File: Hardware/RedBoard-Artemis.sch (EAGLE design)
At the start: 84 parts, among them IC3 LM1117, J2 CORTEX_DEBUG, J3 POWER_JACKTOE, J5 USB-C, Q1 1.1A/60V/600mΩ, U1 ARTEMIS_MODULESMD, U3 AP2112-3.3V, U5 CH340C, Y1 32.768kHz

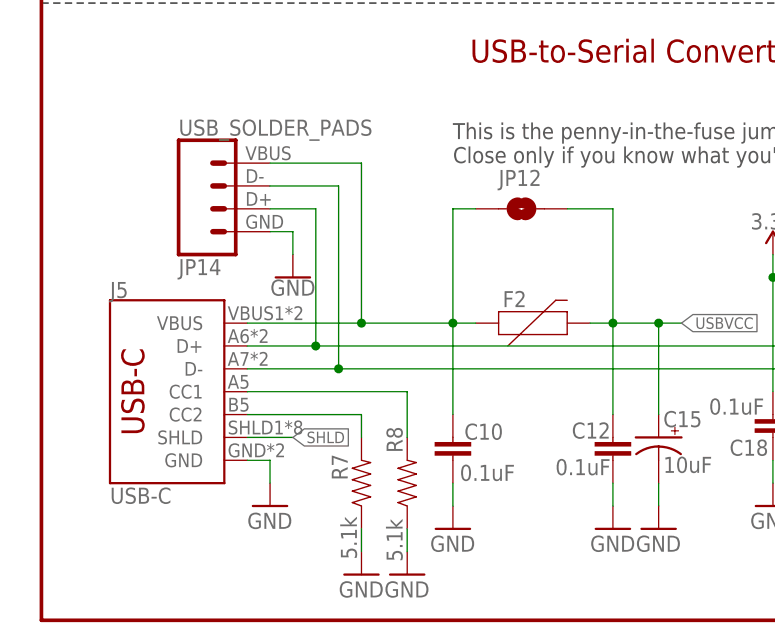
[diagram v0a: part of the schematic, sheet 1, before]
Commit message: Move measurement PTH from under CR2032.
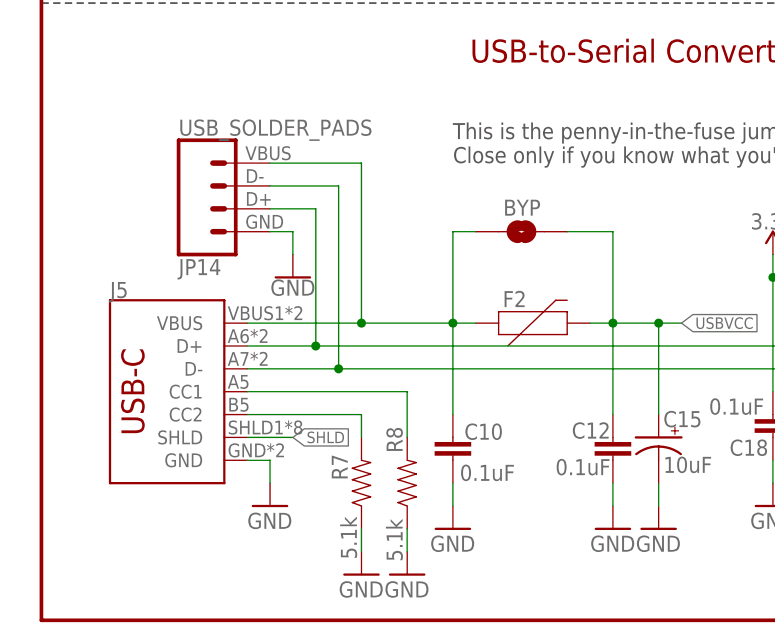
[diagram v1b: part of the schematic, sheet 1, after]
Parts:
- removed JP12: JUMPER-SMT_2_NO_SILK, SparkFun-Jumpers:JUMPER-SMT_2_NO_SILK
- added BYP: JUMPER-SMT_2_NO_SILK, SparkFun-Jumpers:JUMPER-SMT_2_NO_SILK
- J5: device SparkFun-Connectors:USB_C -> SparkFun-Connectors:USB_C2-LAYER
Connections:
- net USBVCC: now also BYP.2; no longer JP12.2
- net VUSB: now also BYP.1; no longer JP12.1
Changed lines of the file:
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@@
 <part name="R16" library="SparkFun-Resistors" deviceset="4.7KOHM" device="-0603-1/10W-1%" value="4.7k"/>
 <part name="D2" library="SparkFun-LED" deviceset="LED-GREEN" device="LILYPAD" value="GREEN"/>
-<part name="J5" library="SparkFun-Connectors" deviceset="USB_C" device="" value="USB-C"/>
+<part name="J5" library="SparkFun-Connectors" deviceset="USB_C" device="2-LAYER" value="USB-C"/>
 <part name="GND38" library="SparkFun-PowerSymbols" deviceset="GND" device=""/>
 <part name="U5" library="SparkFun-IC-Comms" deviceset="CH340C" device=""/>
@@
 <part name="JP14" library="SparkFun-Connectors" deviceset="USB_SOLDER_PADS" device=""/>
 <part name="GND17" library="SparkFun-PowerSymbols" deviceset="GND" device=""/>
-<part name="JP12" library="SparkFun-Jumpers" deviceset="JUMPER-SMT_2_NO" device="_SILK" value=""/>
+<part name="BYP" library="SparkFun-Jumpers" deviceset="JUMPER-SMT_2_NO" device="_SILK" value=""/>
 <part name="F2" library="SparkFun-Fuses" deviceset="PPTC" device="_6V2A" value="6V/2A"/>
 <part name="GND6" library="SparkFun-PowerSymbols" deviceset="GND" device=""/>
@@
 </instance>
 <instance part="J5" gate="J1" x="10.16" y="25.4" smashed="yes">
-<attribute name="VALUE" x="7.62" y="12.954" size="1.778" layer="96" font="vector" rot="MR180" align="top-left"/>
 <attribute name="NAME" x="7.62" y="35.814" size="1.778" layer="95" font="vector"/>
 </instance>
@@
 <attribute name="VALUE" x="27.94" y="37.846" size="1.778" layer="96" align="top-center"/>
 </instance>
-<instance part="JP12" gate="G$1" x="53.34" y="45.72" smashed="yes">
-<attribute name="NAME" x="50.8" y="48.26" size="1.778" layer="95" font="vector"/>
+<instance part="BYP" gate="G$1" x="53.34" y="43.18" smashed="yes">
+<attribute name="NAME" x="51.308" y="44.958" size="1.778" layer="95" font="vector"/>
 </instance>
 <instance part="F2" gate="F1" x="53.34" y="33.02" smashed="yes">
@@
 <wire x1="68.58" y1="33.02" x2="71.12" y2="33.02" width="0.1524" layer="91"/>
 <junction x="68.58" y="33.02"/>
-<pinref part="JP12" gate="G$1" pin="2"/>
-<wire x1="58.42" y1="45.72" x2="63.5" y2="45.72" width="0.1524" layer="91"/>
-<wire x1="63.5" y1="45.72" x2="63.5" y2="33.02" width="0.1524" layer="91"/>
+<pinref part="BYP" gate="G$1" pin="2"/>
+<wire x1="58.42" y1="43.18" x2="63.5" y2="43.18" width="0.1524" layer="91"/>
+<wire x1="63.5" y1="43.18" x2="63.5" y2="33.02" width="0.1524" layer="91"/>
 <pinref part="F2" gate="F1" pin="2"/>
 </segment>
@@
 <wire x1="35.56" y1="50.8" x2="35.56" y2="33.02" width="0.1524" layer="91"/>
 <junction x="35.56" y="33.02"/>
-<pinref part="JP12" gate="G$1" pin="1"/>
-<wire x1="48.26" y1="45.72" x2="45.72" y2="45.72" width="0.1524" layer="91"/>
-<wire x1="45.72" y1="45.72" x2="45.72" y2="33.02" width="0.1524" layer="91"/>
+<pinref part="BYP" gate="G$1" pin="1"/>
+<wire x1="48.26" y1="43.18" x2="45.72" y2="43.18" width="0.1524" layer="91"/>
+<wire x1="45.72" y1="43.18" x2="45.72" y2="33.02" width="0.1524" layer="91"/>
 <pinref part="F2" gate="F1" pin="1"/>
 </segment>

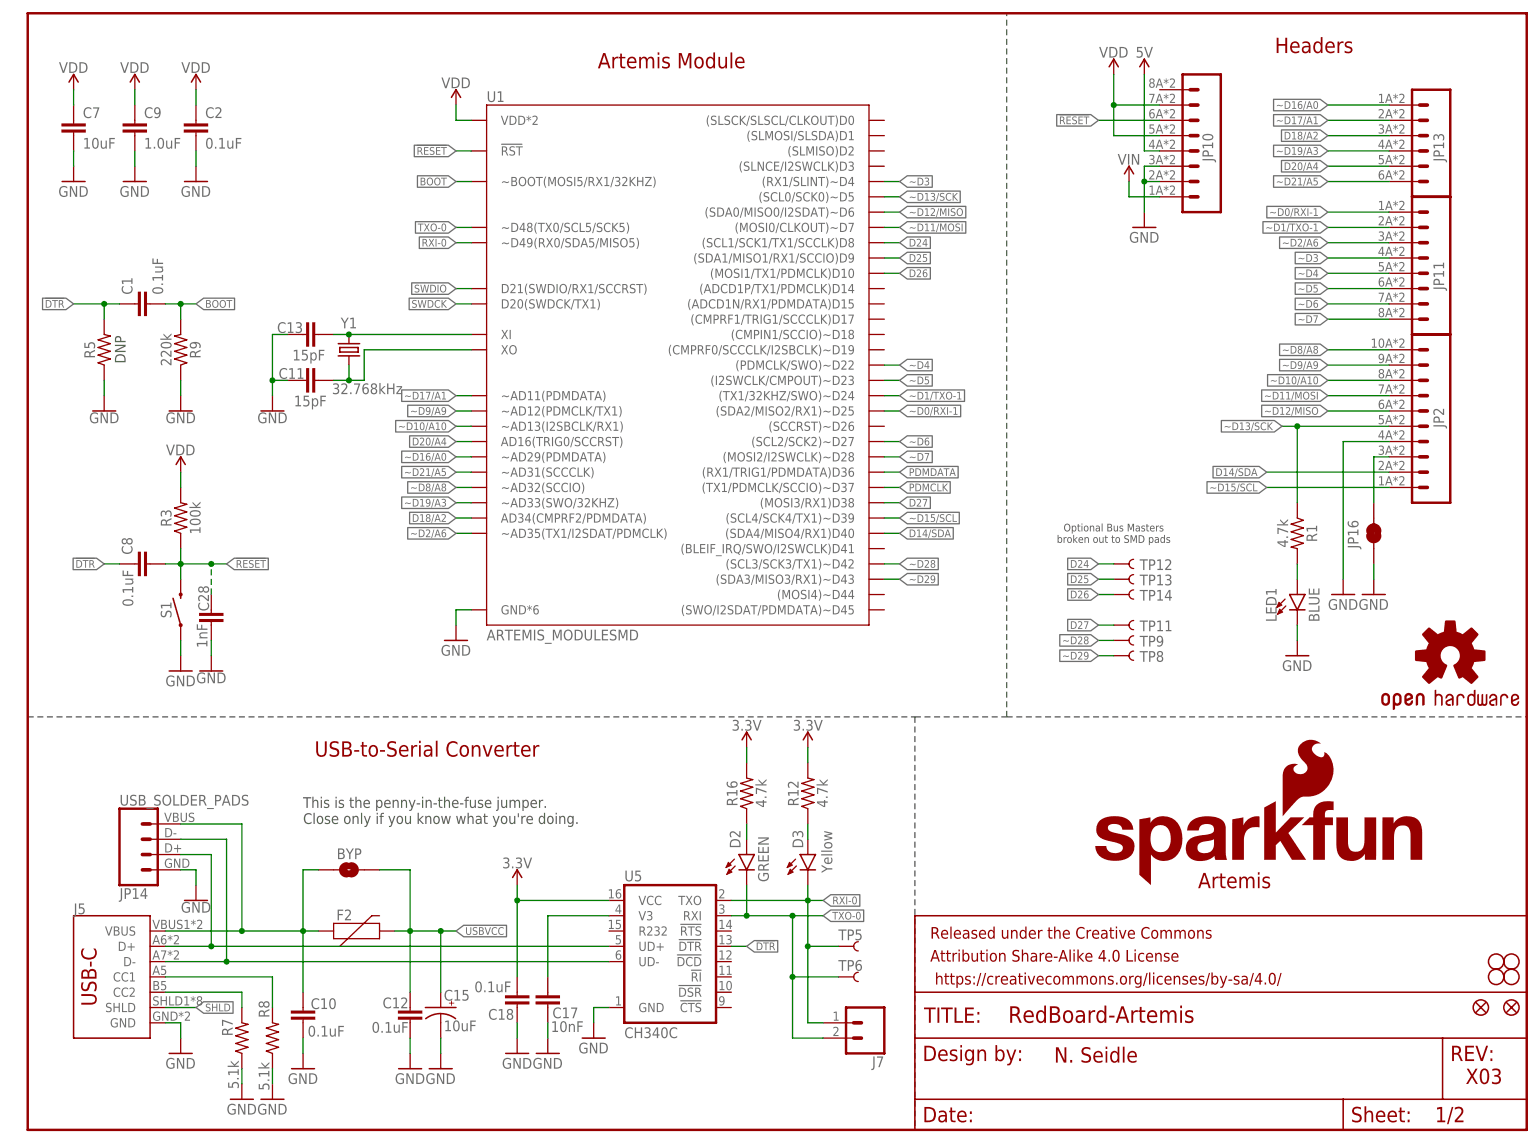
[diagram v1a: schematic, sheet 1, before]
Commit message: Rename silk to RedBoard. Change version to v10.
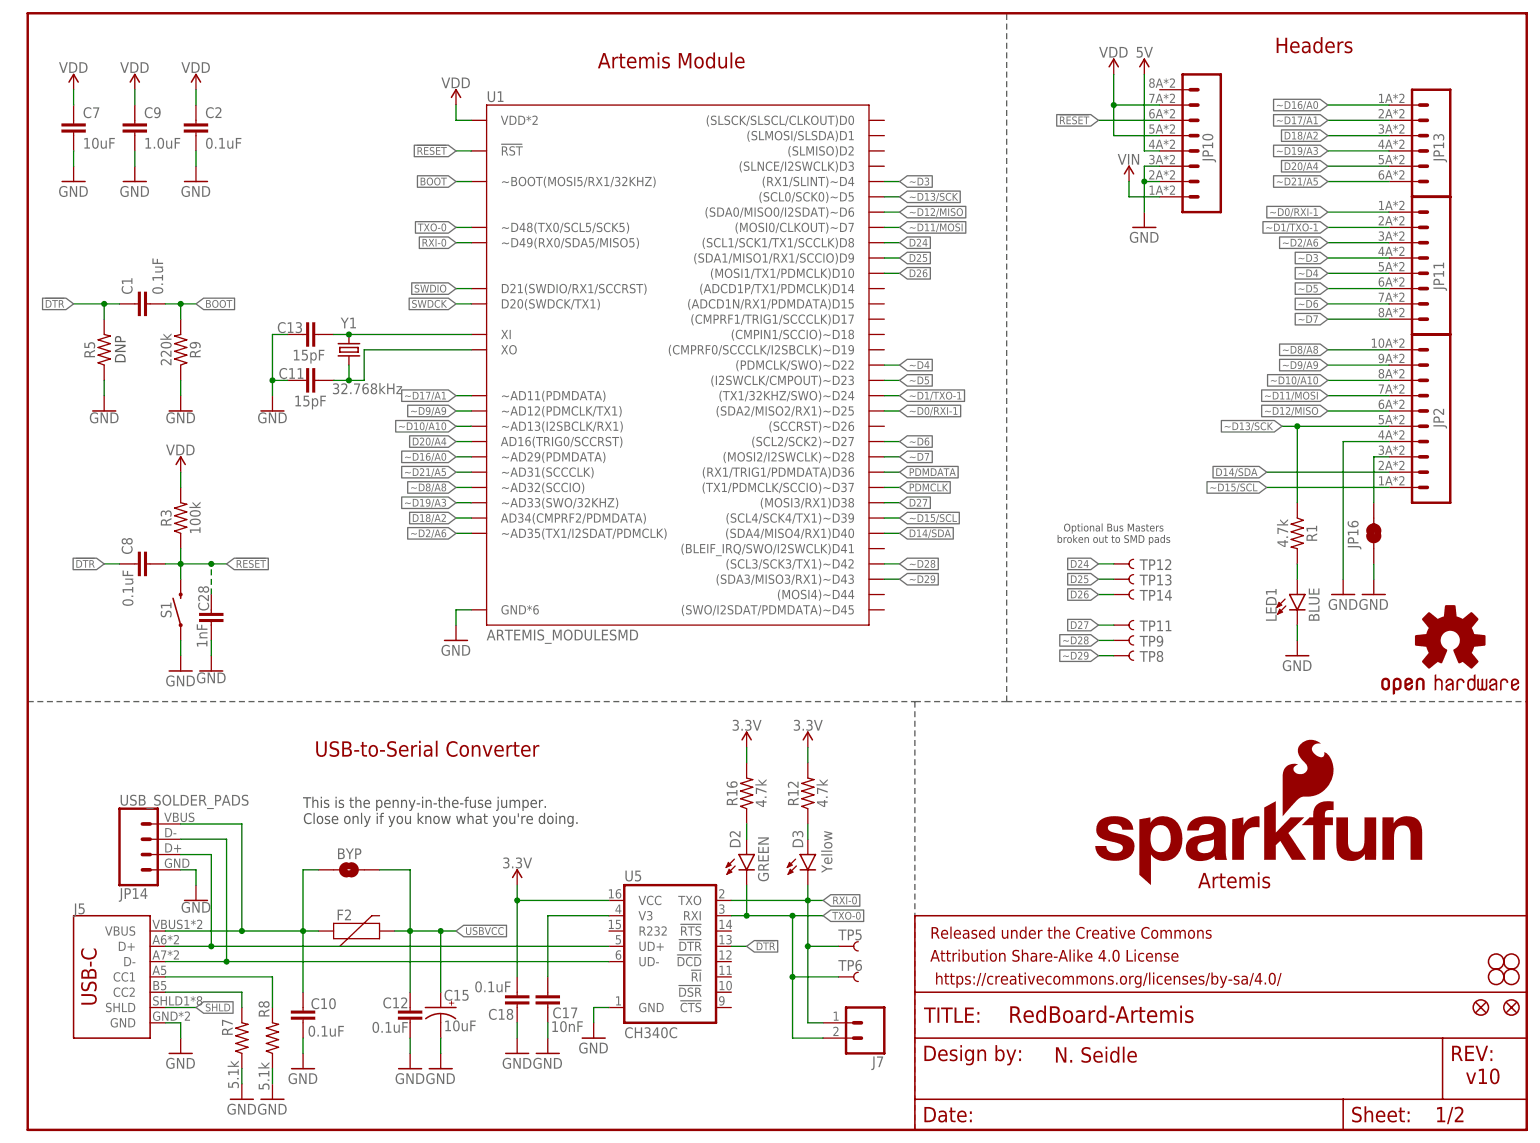
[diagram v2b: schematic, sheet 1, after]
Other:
- note added: "v10"
- note removed: "X03"
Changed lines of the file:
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@@
 <sheet>
 <plain>
-<wire x1="0" y1="68.58" x2="147.32" y2="68.58" width="0.2032" layer="97" style="longdash"/>
+<wire x1="0" y1="71.12" x2="147.32" y2="71.12" width="0.2032" layer="97" style="longdash"/>
 <text x="200.406" y="41.402" size="2.54" layer="94" font="vector" ratio="15" align="center">Artemis</text>
 <text x="66.294" y="63.246" size="2.54" layer="94" font="vector" ratio="15" align="center">USB-to-Serial Converter</text>
 <text x="170.434" y="11.176" size="2.54" layer="94" font="vector">N. Seidle</text>
-<text x="238.76" y="7.62" size="2.54" layer="94" font="vector">X03</text>
-<wire x1="147.32" y1="68.58" x2="162.56" y2="68.58" width="0.2032" layer="97" style="longdash"/>
-<wire x1="162.56" y1="68.58" x2="248.92" y2="68.58" width="0.2032" layer="97" style="longdash"/>
-<wire x1="147.32" y1="68.58" x2="147.32" y2="0" width="0.2032" layer="97" style="longdash"/>
+<text x="238.76" y="7.62" size="2.54" layer="94" font="vector">v10</text>
+<wire x1="147.32" y1="71.12" x2="162.56" y2="71.12" width="0.2032" layer="97" style="longdash"/>
+<wire x1="162.56" y1="71.12" x2="248.92" y2="71.12" width="0.2032" layer="97" style="longdash"/>
+<wire x1="147.32" y1="71.12" x2="147.32" y2="0" width="0.2032" layer="97" style="longdash"/>
 <text x="45.72" y="50.8" size="1.778" layer="97" font="vector">This is the penny-in-the-fuse jumper.
 Close only if you know what you're doing.</text>
@@
 <text x="106.934" y="177.546" size="2.54" layer="94" font="vector" ratio="15" align="center">Artemis Module</text>
 <text x="213.614" y="180.086" size="2.54" layer="94" font="vector" ratio="15" align="center">Headers</text>
-<wire x1="162.56" y1="68.58" x2="162.56" y2="185.42" width="0.2032" layer="97" style="longdash"/>
+<wire x1="162.56" y1="71.12" x2="162.56" y2="185.42" width="0.2032" layer="97" style="longdash"/>
 <text x="16.256" y="127.254" size="1.778" layer="97" rot="R90">DNP</text>
 </plain>
@@
 <instance part="JP8" gate="G$1" x="241.3" y="20.32" smashed="yes"/>
 <instance part="JP9" gate="G$1" x="246.38" y="20.32" smashed="yes"/>
-<instance part="U$16" gate="G$1" x="236.22" y="78.74" smashed="yes"/>
+<instance part="U$16" gate="G$1" x="236.22" y="81.28" smashed="yes"/>
 <instance part="C12" gate="G$1" x="63.5" y="17.78" smashed="yes" rot="MR0">
 <attribute name="NAME" x="63.246" y="20.193" size="1.778" layer="95" font="vector" rot="MR0"/>
